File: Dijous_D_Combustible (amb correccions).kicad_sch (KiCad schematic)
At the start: 55 parts, among them J1 Conn_01x02, J2 DE9_Plug, J4 Conn_02x03_Counter_Clockwise, J5 Screw_Terminal_01x02, K1 Fujitsu_FTR-LYAA005x, K2 Fujitsu_FTR-LYAA005x, Q1 2SC4213, Q2 2SC4213, U1 LM2596S-ADJ, U3 MCP2551-I-SN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

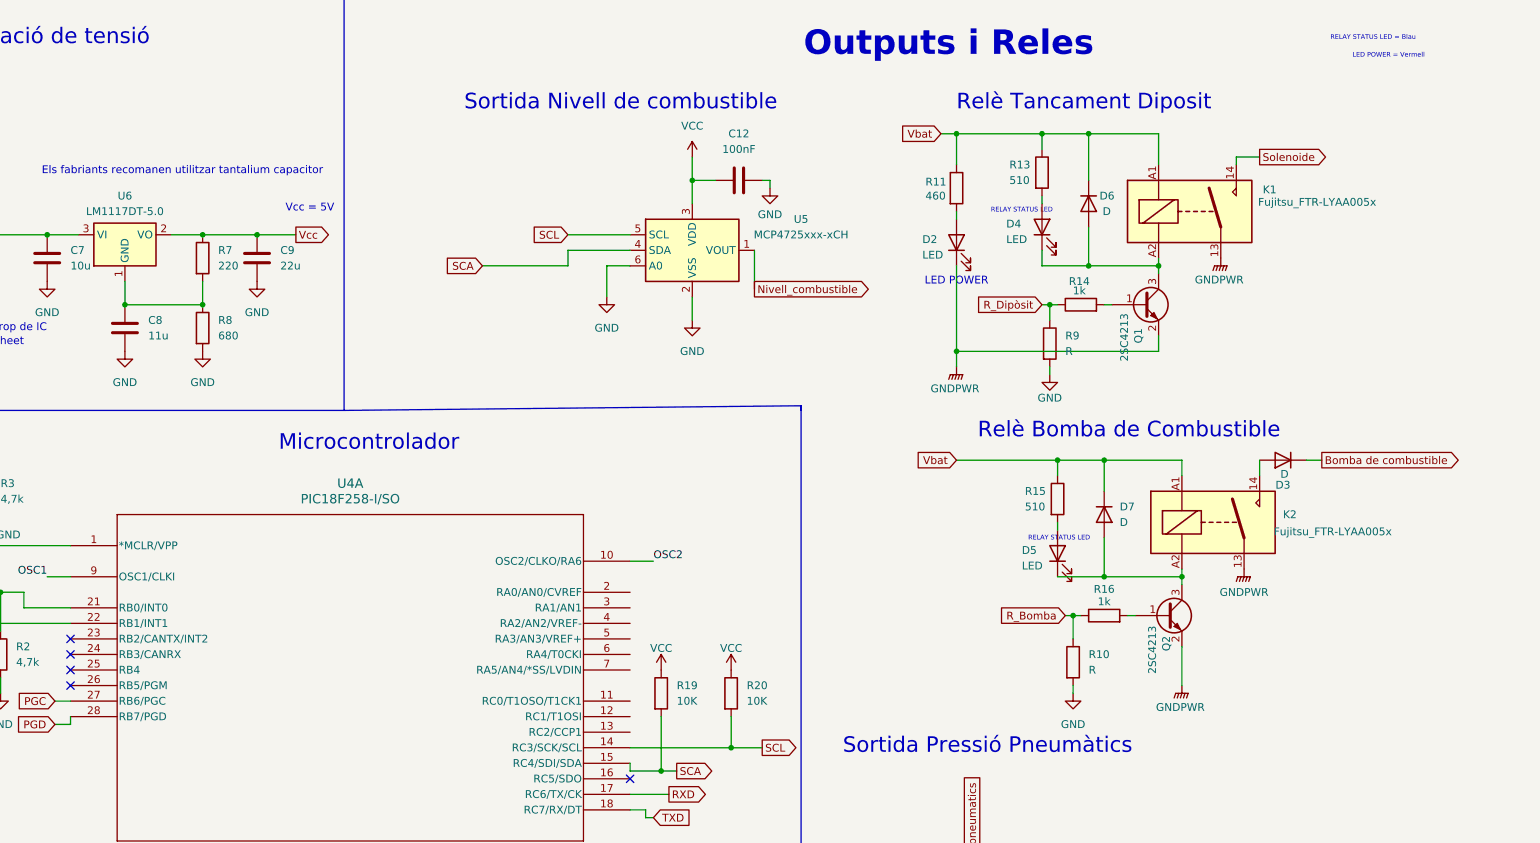
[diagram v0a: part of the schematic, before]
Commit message: README i kicad.sch
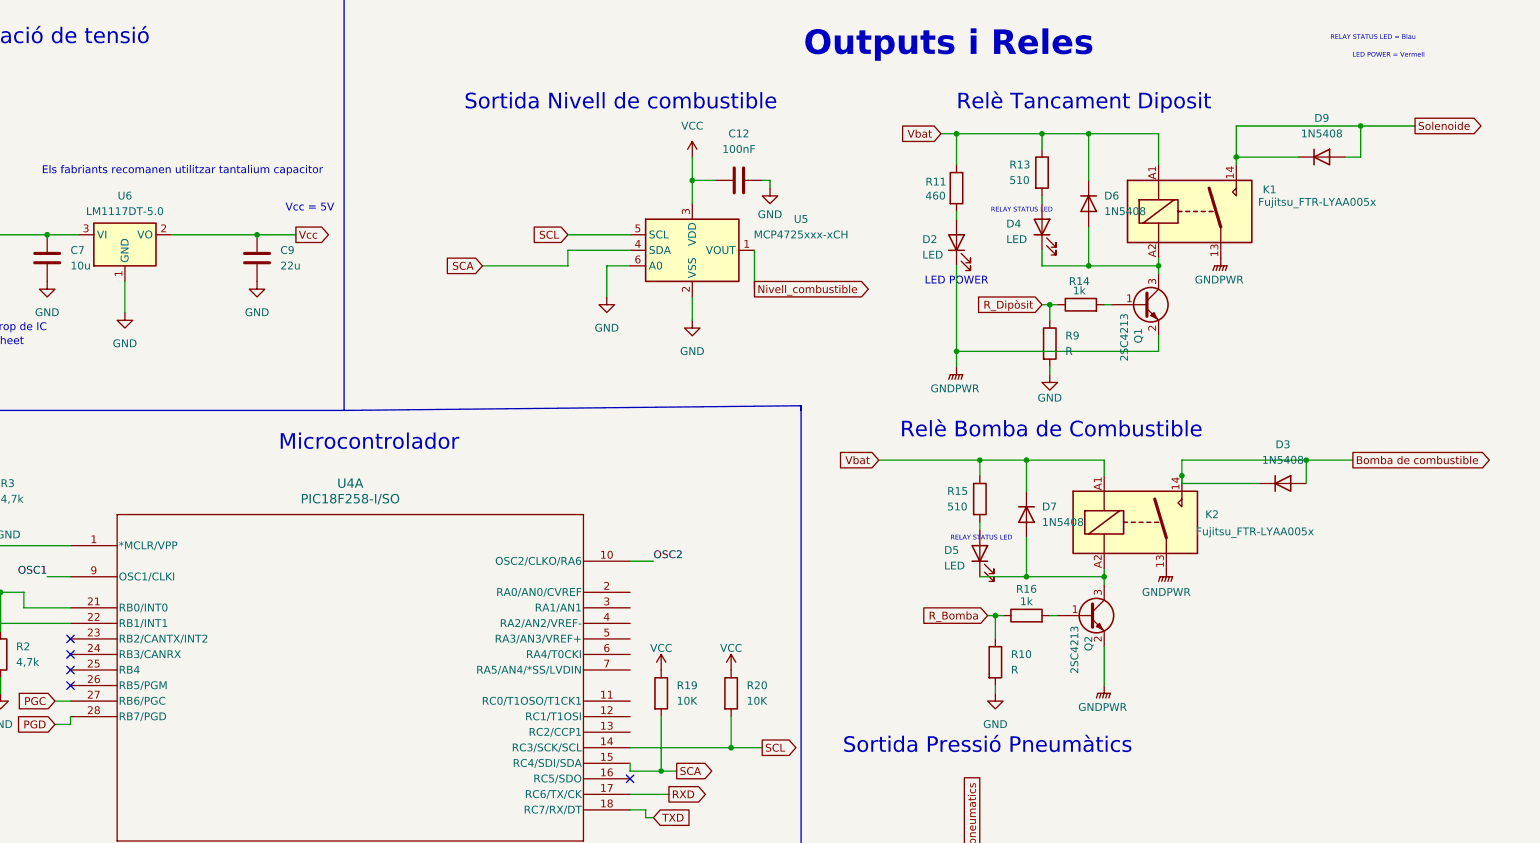
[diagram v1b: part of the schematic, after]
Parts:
- removed C8: 11u, symbol Device:C
- removed D3, D6, D7: D, symbol Device:D
- removed R7: 220, symbol Device:R
- removed R8: 680, symbol Device:R
- added D3, D6, D7, D9: 1N5408, Diode_THT:D_DO-201AD_P15.24mm_Horizontal, symbol Diode:1N5408
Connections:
- net Bomba de combustible: now also K2.14, D3.1 (K), D3.2 (A)
- net GND: now also U6.1 (GND)
- net Solenoide: now also D9.1 (K), D9.2 (A)
- net Vbat: now also D6.1 (K), D7.1 (K)
- net at D4.1 (K), K1.A2, Q1.3 (C): now also D6.2 (A)
- net at D5.1 (K), K2.A2, Q2.3 (C): now also D7.2 (A)
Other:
- moved on the sheet: D5, K2, Q2, R10, R15, R16

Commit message: Esquematic
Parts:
- removed J5: Screw_Terminal_01x02, symbol Connector:Screw_Terminal_01x02
- added J3: Screw_Terminal_01x02, TerminalBlock:TerminalBlock_Altech_AK300-2_P5.00mm, symbol Connector:Screw_Terminal_01x02
- J1: footprint (none) -> Connector_PinHeader_2.00mm:PinHeader_2x01_P2.00mm_Vertical
- J2: footprint (none) -> Connector_Dsub:DSUB-9_Male_Vertical_P2.77x2.84mm
- J4: footprint (none) -> Connector_PinHeader_2.54mm:PinHeader_2x03_P2.54mm_Vertical
- L1: footprint (none) -> Inductor_SMD:L_1206_3216Metric
- R1, R10, R11, R12, R13, R14, R15, R16, R17, R18, R19, R2, R20, R3, R4, R5, R6, R9: footprint (none) -> Resistor_SMD:R_1206_3216Metric
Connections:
- net GNDPWR: now also J3.1 (Pin_1)
- net Vbat: now also J3.2 (Pin_2); no longer C4.1, R5.2, U1.1 (VIN)
- new net: C4.1, R5.2, U1.1 (VIN)
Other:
- note removed: "Condensador datasheet"
- note removed: "Condensador:"
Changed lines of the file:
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@@
 	(wire
 		(pts
-			(xy 80.01 45.72) (xy 83.82 45.72)
-		)
-		(stroke
-			(width 0)
-			(type default)
-		)
-	)
-	(wire
-		(pts
 			(xy 316.23 46.99) (xy 316.23 48.26)
 		)
@@
 		)
 	)
-	(text "Condensador: "
-		(exclude_from_sim no)
-		(at 77.978 65.532 0)
-		(effects
-			(font
-				(size 1.27 1.27)
-			)
-			(href "https://www.vishay.com/docs/28323/150rmi.pdf")
-		)
-	)
 	(text "Conector botó apertura \nde combustible o tancament"
 		(exclude_from_sim no)
@@
 		)
 	)
-	(text "Condensador datasheet\n"
-		(exclude_from_sim no)
-		(at 153.416 68.326 0)
-		(effects
-			(font
-				(size 1.27 1.27)
-			)
-			(href "https://eu.mouser.com/datasheet/2/293/e_ucz-1903374.pdf")
-		)
-	)
 	(text "Els fabriants recomanen utilitzar tantalium capacitor"
 		(exclude_from_sim no)
@@
 	(global_label "Vbat"
 		(shape input)
-		(at 80.01 45.72 180)
+		(at 71.12 45.72 180)
 		(fields_autoplaced yes)
 		(effects
@@
 		)
 		(property "Intersheetrefs" "${INTERSHEET_REFS}"
-			(at 72.9125 45.72 0)
+			(at 64.0225 45.72 0)
 			(effects
 				(font
@@
 			)
 		)
-		(property "Footprint" ""
+		(property "Footprint" "Resistor_SMD:R_1206_3216Metric"
 			(at 327.66 114.808 90)
 			(effects
@@
 			)
 		)
-		(property "Footprint" ""
+		(property "Footprint" "Resistor_SMD:R_1206_3216Metric"
 			(at 336.55 64.008 90)
 			(effects
@@
 			)
 		)
-		(property "Footprint" ""
+		(property "Footprint" "Resistor_SMD:R_1206_3216Metric"
 			(at 75.692 163.83 90)
 			(effects
@@
 			)
 		)
-		(property "Footprint" ""
+		(property "Footprint" "Resistor_SMD:R_1206_3216Metric"
 			(at 266.192 125.73 90)
 			(effects
@@
 			)
 		)
-		(property "Footprint" ""
+		(property "Footprint" "Resistor_SMD:R_1206_3216Metric"
 			(at 316.992 179.07 90)
 			(effects
@@
 			)
 		)
-		(property "Footprint" ""
+		(property "Footprint" "Resistor_SMD:R_1206_3216Metric"
 			(at 329.692 68.58 90)
 			(effects
@@
 			)
 		)
-		(property "Footprint" ""
+		(property "Footprint" "Resistor_SMD:R_1206_3216Metric"
 			(at 75.692 171.45 90)
 			(effects
@@
 			)
 		)
-		(property "Footprint" ""
+		(property "Footprint" "Resistor_SMD:R_1206_3216Metric"
 			(at 42.672 179.07 90)
 			(effects
@@
 	)
 	(symbol
-		(lib_id "Connector:Screw_Terminal_01x02")
-		(at 29.21 43.18 180)
-		(unit 1)
-		(exclude_from_sim no)
-		(in_bom yes)
-		(on_board yes)
-		(dnp no)
-		(property "Reference" "J5"
-			(at 29.21 34.29 0)
-			(effects
-				(font
-					(size 1.27 1.27)
-				)
-			)
-		)
-		(property "Value" "Screw_Terminal_01x02"
-			(at 26.924 36.322 0)
-			(effects
-				(font
-					(size 1.27 1.27)
-				)
-			)
-		)
-		(property "Footprint" ""
-			(at 29.21 43.18 0)
-			(effects
-				(font
-					(size 1.27 1.27)
-				)
-				(hide yes)
-			)
-		)
-		(property "Datasheet" "~"
-			(at 29.21 43.18 0)
-			(effects
-				(font
-					(size 1.27 1.27)
-				)
-				(hide yes)
-			)
-		)
-		(property "Description" "Generic screw terminal, single row, 01x02, script generated (kicad-library-utils/schlib/autogen/connector/)"
-			(at 29.21 43.18 0)
-			(effects
-				(font
-					(size 1.27 1.27)
-				)
-				(hide yes)
-			)
-		)
-		(pin "1"
-		)
-		(pin "2"
-		)
-		(instances
-			(project ""
-				(path "/8e5e5a45-9171-45b6-b00a-10c0ac4f5428"
-					(reference "J5")
-					(unit 1)
-				)
-			)
-		)
-	)
-	(symbol
 		(lib_id "power:GND")
 		(at 144.78 58.42 0)
@@
 			)
 		)
-		(property "Footprint" ""
+		(property "Footprint" "Resistor_SMD:R_1206_3216Metric"
 			(at 155.702 92.71 90)
 			(effects
@@
 			)
 		)
-		(property "Footprint" ""
+		(property "Footprint" "Resistor_SMD:R_1206_3216Metric"
 			(at 277.622 125.73 90)
 			(effects
@@
 			)
 		)
-		(property "Footprint" ""
+		(property "Footprint" "Connector_PinHeader_2.00mm:PinHeader_2x01_P2.00mm_Vertical"
 			(at 33.02 71.12 0)
 			(effects
@@
 			)
 		)
-		(property "Footprint" ""
+		(property "Footprint" "Inductor_SMD:L_1206_3216Metric"
 			(at 135.89 50.8 0)
 			(effects
@@
 			)
 		)
-		(property "Footprint" ""
+		(property "Footprint" "Resistor_SMD:R_1206_3216Metric"
 			(at 314.452 43.18 90)
 			(effects
@@
 		(fields_autoplaced yes)
 		(property "Reference" "J2"
-			(at 129.54 181.61 0)
+			(at 134.62 162.5599 0)
 			(effects
 				(font
 					(size 1.27 1.27)
 				)
+				(justify left)
 			)
 		)
 		(property "Value" "DE9_Plug"
-			(at 129.54 179.07 0)
+			(at 134.62 165.0999 0)
 			(effects
 				(font
 					(size 1.27 1.27)
 				)
+				(justify left)
 			)
 		)
-		(property "Footprint" ""
+		(property "Footprint" "Connector_Dsub:DSUB-9_Male_Vertical_P2.77x2.84mm"
 			(at 129.54 163.83 0)
 			(effects
@@
 			)
 		)
-		(property "Footprint" ""
+		(property "Footprint" "Connector_PinHeader_2.54mm:PinHeader_2x03_P2.54mm_Vertical"
 			(at 36.83 99.06 0)
 			(effects
@@
 			)
 		)
-		(property "Footprint" ""
+		(property "Footprint" "Resistor_SMD:R_1206_3216Metric"
 			(at 320.802 120.65 90)
 			(effects
@@
 			)
 		)
-		(property "Footprint" ""
+		(property "Footprint" "Resistor_SMD:R_1206_3216Metric"
 			(at 158.242 119.38 90)
 			(effects
@@
 	)
 	(symbol
+		(lib_id "Connector:Screw_Terminal_01x02")
+		(at 29.21 43.18 180)
+		(unit 1)
+		(exclude_from_sim no)
+		(in_bom yes)
+		(on_board yes)
+		(dnp no)
+		(fields_autoplaced yes)
+		(property "Reference" "J3"
+			(at 29.21 34.29 0)
+			(effects
+				(font
+					(size 1.27 1.27)
+				)
+			)
+		)
+		(property "Value" "Screw_Terminal_01x02"
+			(at 29.21 36.83 0)
+			(effects
+				(font
+					(size 1.27 1.27)
+				)
+			)
+		)
+		(property "Footprint" "TerminalBlock:TerminalBlock_Altech_AK300-2_P5.00mm"
+			(at 29.21 43.18 0)
+			(effects
+				(font
+					(size 1.27 1.27)
+				)
+				(hide yes)
+			)
+		)
+		(property "Datasheet" "~"
+			(at 29.21 43.18 0)
+			(effects
+				(font
+					(size 1.27 1.27)
+				)
+				(hide yes)
+			)
+		)
+		(property "Description" "Generic screw terminal, single row, 01x02, script generated (kicad-library-utils/schlib/autogen/connector/)"
+			(at 29.21 43.18 0)
+			(effects
+				(font
+					(size 1.27 1.27)
+				)
+				(hide yes)
+			)
+		)
+		(pin "1"
+		)
+		(pin "2"
+		)
+		(instances
+			(project ""
+				(path "/8e5e5a45-9171-45b6-b00a-10c0ac4f5428"
+					(reference "J3")
+					(unit 1)
+				)
+			)
+		)
+	)
+	(symbol
 		(lib_id "power:VCC")
 		(at 279.4 121.92 0)
@@
 			)
 		)
-		(property "Footprint" ""
+		(property "Footprint" "Resistor_SMD:R_1206_3216Metric"
 			(at 102.87 32.512 90)
 			(effects
@@
 			)
 		)
-		(property "Footprint" ""
+		(property "Footprint" "Resistor_SMD:R_1206_3216Metric"
 			(at 328.422 40.64 90)
 			(effects
@@
 			)
 		)
-		(property "Footprint" ""
+		(property "Footprint" "Resistor_SMD:R_1206_3216Metric"
 			(at 82.55 19.812 90)
 			(effects
@@
 			)
 		)
-		(property "Footprint" ""
+		(property "Footprint" "Resistor_SMD:R_1206_3216Metric"
 			(at 121.92 36.068 90)
 			(effects
@@
 			)
 		)
-		(property "Footprint" ""
+		(property "Footprint" "Resistor_SMD:R_1206_3216Metric"
 			(at 318.262 93.98 90)
 			(effects
